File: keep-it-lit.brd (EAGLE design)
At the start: 49 x 43.5 mm, 33 parts, among them IC1 74AHCT1G04DBV, Q1 BSS138, Q2 BSS138, Q3 BSS138, Q4 BSS138

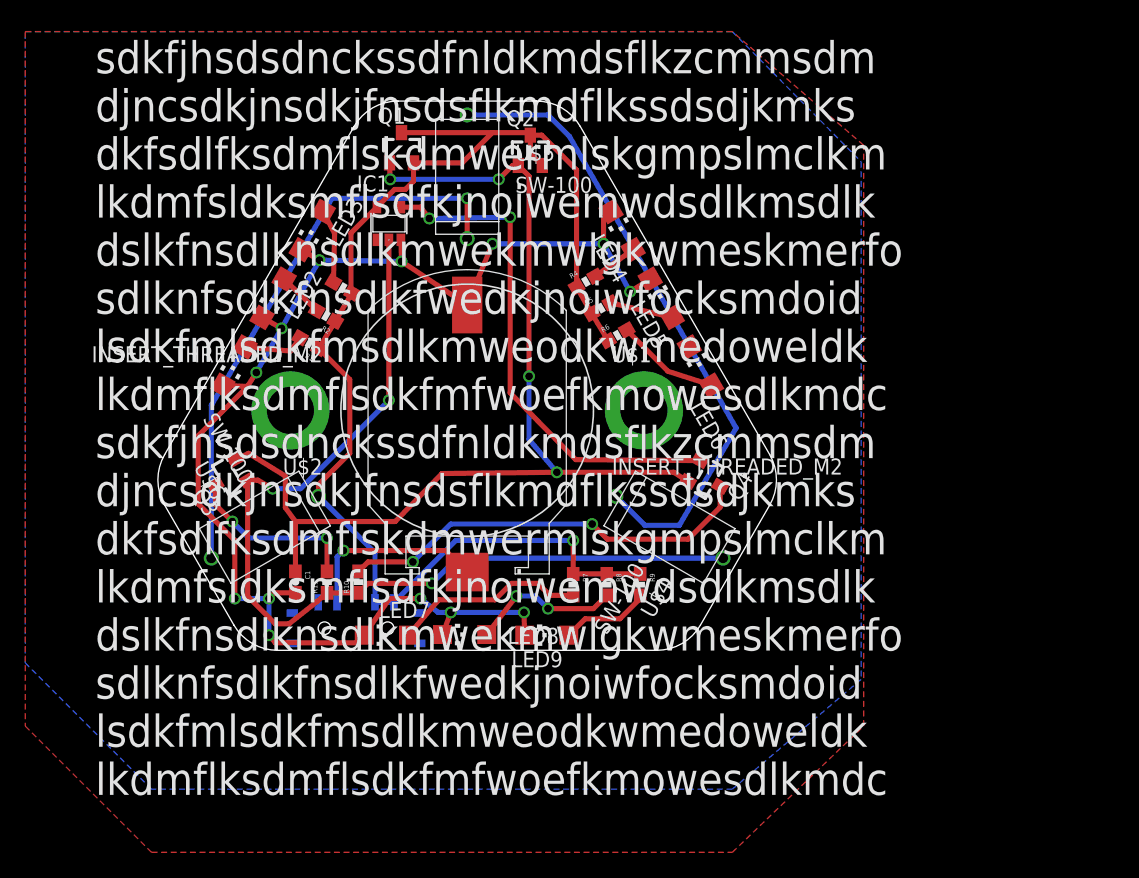
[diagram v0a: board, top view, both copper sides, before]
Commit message: added lib, improved routing, fixed ground plane issues
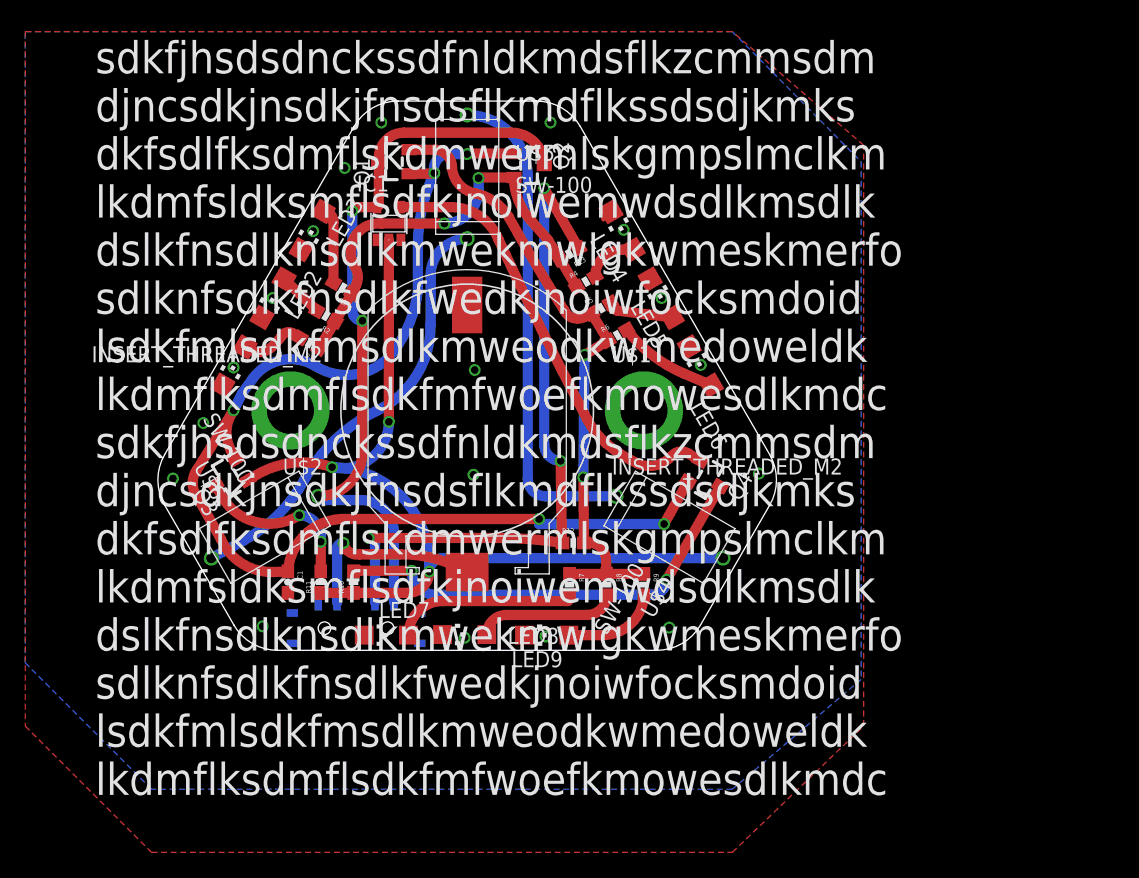
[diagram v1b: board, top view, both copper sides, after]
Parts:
- added R12, R13: (no value), SparkFun-Passives:0603-RES
- moved Q1 1.25 mm to (19.2, 44.7), turned to 90 degrees
- moved Q2 1.20 mm to (29.9, 44.4), turned to 270 degrees
- moved C1 0.60 mm to (10.8, 11.4)
- moved R11 0.50 mm to (13.4, 11.4)
- moved R10 0.40 mm to (16.0, 11.4)
- moved R7 0.30 mm to (33.1, 11.2)
- moved R9 0.30 mm to (39.0, 11.2)
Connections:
- new net LED_GROUP1: Q1.2, R12.2, R5.1, R6.1, R7.1, R8.1, R9.1
- new net LED_GROUP2: Q2.2, R1.1, R13.2, R2.1, R3.1, R4.1
- new net VCC_ALLON: R12.1, R13.1, U$3.B
- net VCC: no longer Q1.2, Q2.2, R1.1, R2.1, R3.1, R4.1, R5.1, R6.1, R7.1, R8.1, R9.1, U$3.B
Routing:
- net GND: track 108.2 -> 1.62 mm, vias 13 -> 18
- net VCC_ALLON: track 0.00 -> 55.3 mm, vias 0 -> 3
- net LED_GROUP1: track 0.00 -> 49.8 mm, vias 0 -> 2
- net VCC: track 107.0 -> 58.1 mm, vias 1 -> 2
- net LED_GROUP2: track 0.00 -> 33.9 mm, vias 0 -> 2
- net N$21: track 82.6 -> 95.3 mm, vias 4 -> 5
- net N$11: track 50.3 -> 38.3 mm
- net N$12: track 45.0 -> 33.7 mm, vias 1 -> 0
- net N$13: track 76.7 -> 71.4 mm
- net N$16: track 40.3 -> 35.0 mm, vias 2 -> 0
- net PWR: track 14.8 -> 16.9 mm
- net N$17: track 14.1 -> 12.5 mm
- net N$19: track 33.4 -> 34.6 mm
- net N$1: track 15.3 -> 14.2 mm
- net N$9: track 11.8 -> 10.8 mm, vias 2 -> 0
